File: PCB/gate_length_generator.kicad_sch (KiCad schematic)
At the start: 12 parts, among them SW2 ON/ON, U2 LM555xN

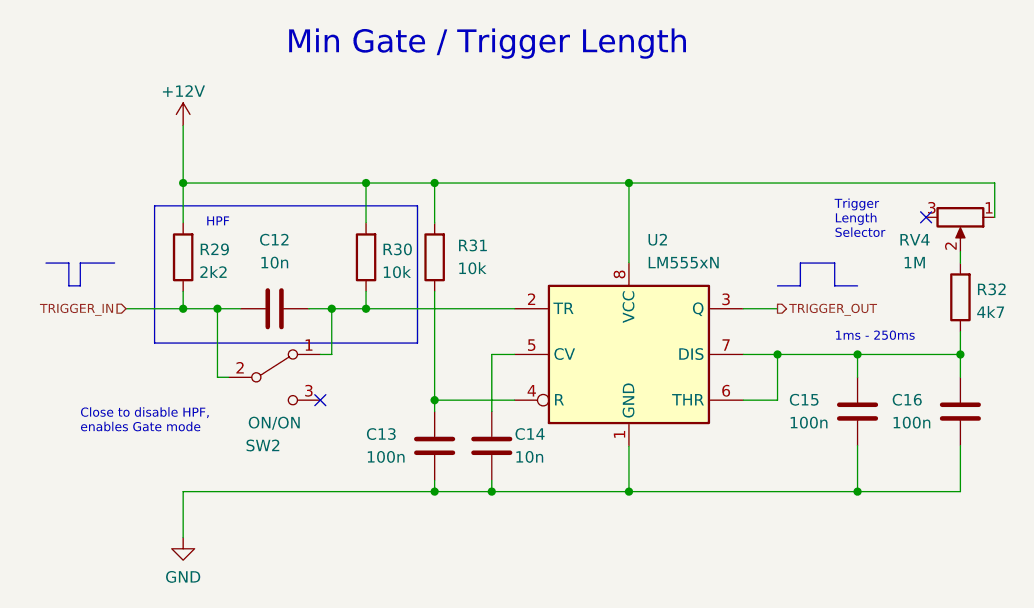
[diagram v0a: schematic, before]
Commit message: :memo: Geographically reannotate the PCB
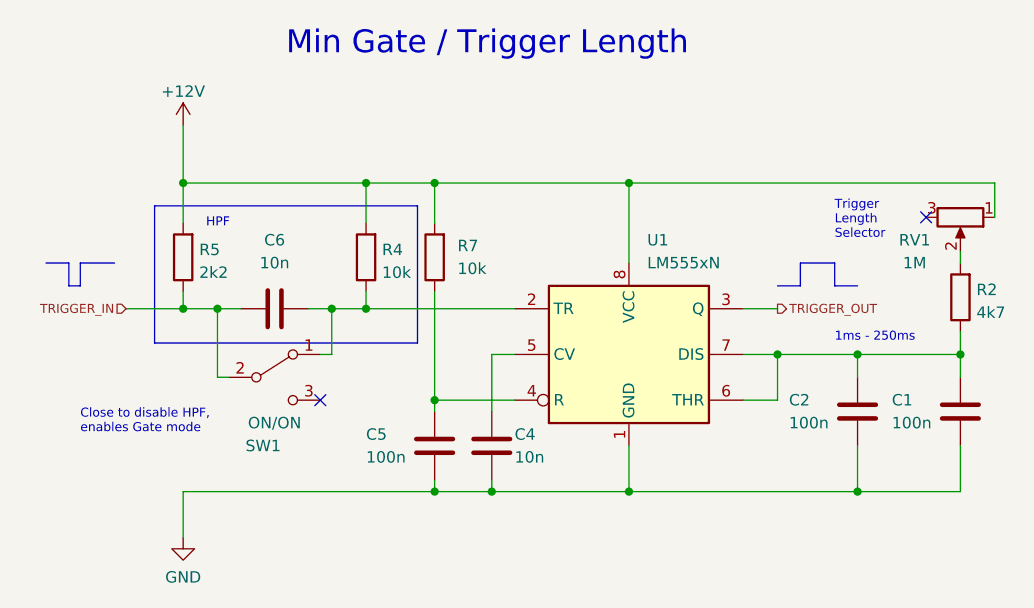
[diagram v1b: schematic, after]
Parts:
- renumbered C16 to C1, C15 to C2, C14 to C4, C13 to C5, C12 to C6, R32 to R2, R30 to R4, R29 to R5, R31 to R7, RV4 to RV1, SW2 to SW1, U2 to U1
